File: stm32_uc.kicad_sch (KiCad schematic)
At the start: 13 parts, among them U1 STM32F103C8T6

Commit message: updated pdb
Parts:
- renumbered U1 to U?
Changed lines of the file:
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@@
   (symbol (lib_id "MCU_ST_STM32F1:STM32F103C8Tx") (at 139.7 100.33 0) (unit 1)
     (in_bom yes) (on_board yes)
-    (property "Reference" "U1" (id 0) (at 149.86 63.5 0)
+    (property "Reference" "U?" (id 0) (at 149.86 63.5 0)
       (effects (font (size 1.27 1.27)) (justify left))
     )
@@
     )
     (path "/780076de-fb73-43f2-b5aa-1c95059ff25d"
-      (reference "U1") (unit 1) (value "STM32F103C8T6") (footprint "Package_QFP:LQFP-48_7x7mm_P0.5mm")
-    )
-  )
+      (reference "U?") (unit 1) (value "STM32F103C8T6") (footprint "Package_QFP:LQFP-48_7x7mm_P0.5mm")
+    )
+  )

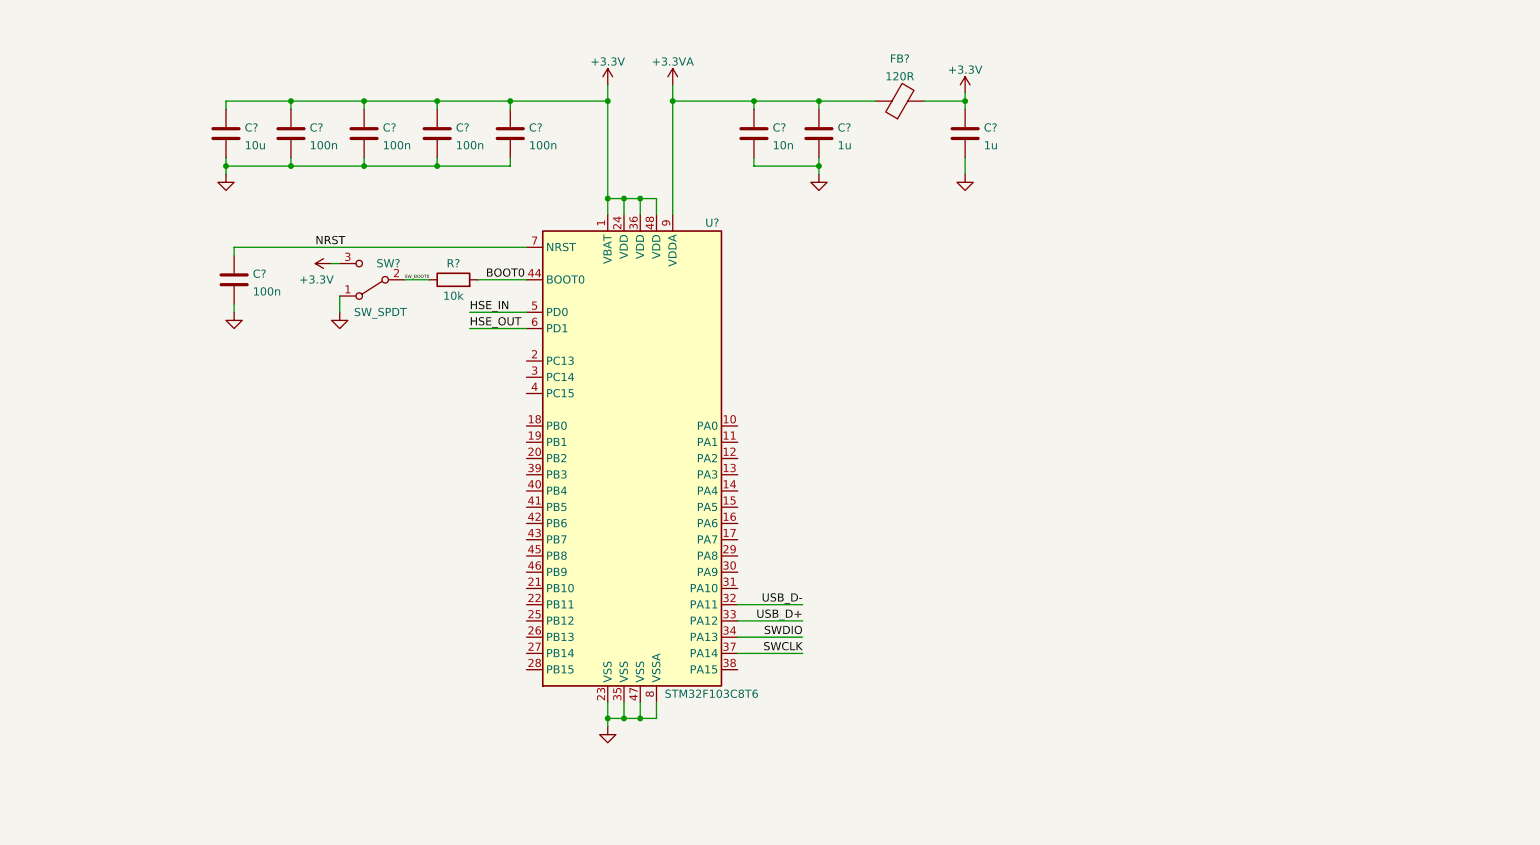
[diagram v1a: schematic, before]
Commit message: added power circuitry
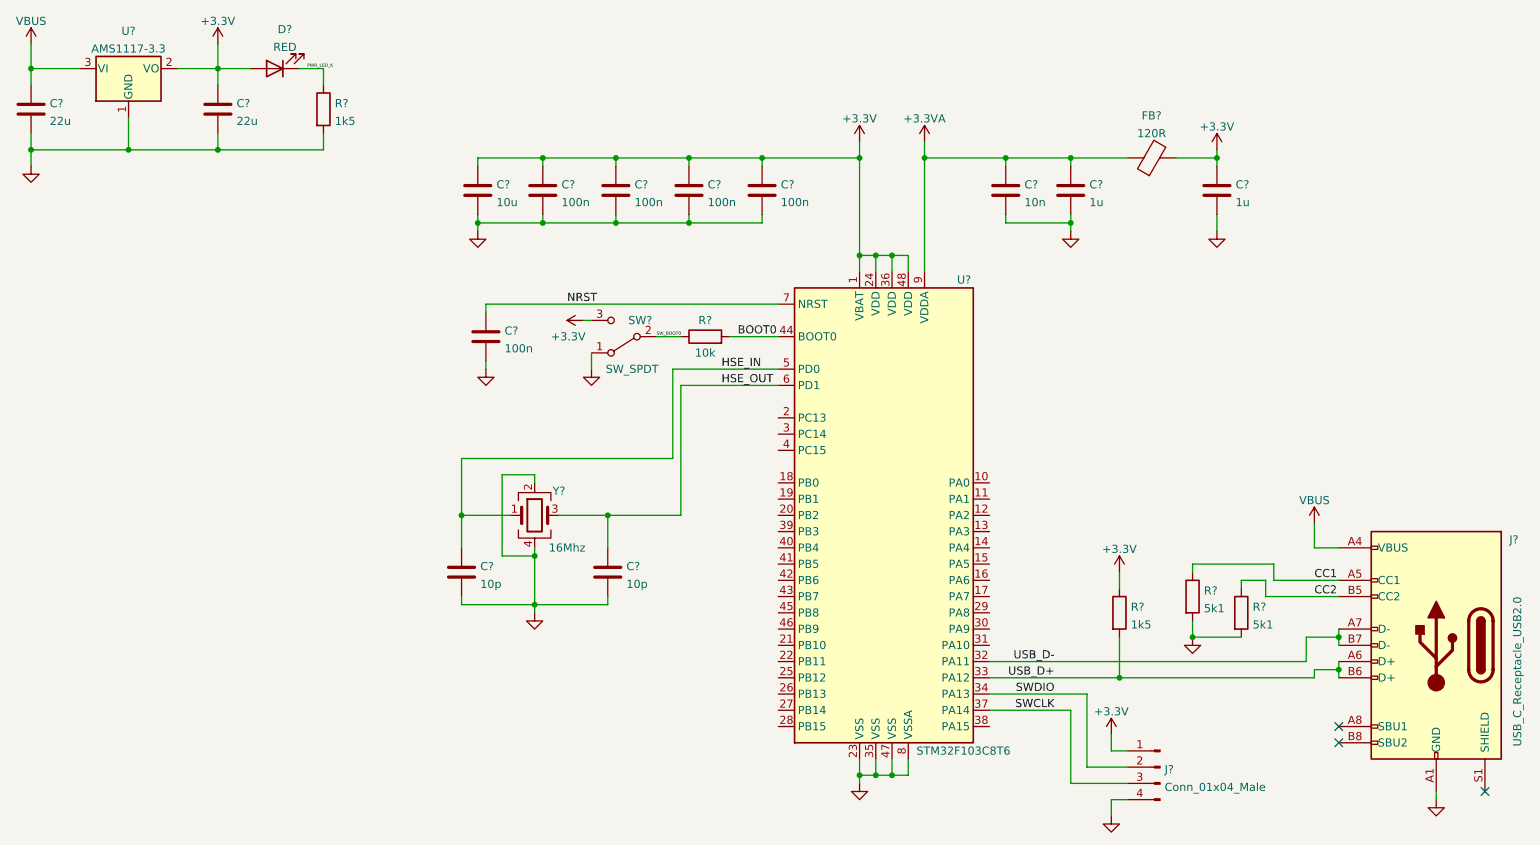
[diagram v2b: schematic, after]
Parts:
- added C? (x2): 22u, symbol Device:C
- added C? (x2): 10p, symbol Device:C
- added D?: RED, symbol Device:LED
- added J?: Conn_01x04_Male, symbol Connector:Conn_01x04_Male
- added J?: USB_C_Receptacle_USB2.0, symbol Connector:USB_C_Receptacle_USB2.0
- added R? (x2): 5k1, symbol Device:R
- added R? (x2): 1k5, symbol Device:R
- added U?: AMS1117-3.3, Package_TO_SOT_SMD:SOT-223-3_TabPin2, symbol Regulator_Linear:AMS1117-3.3
- added Y?: 16Mhz, symbol Device:Crystal_GND24
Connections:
- net +3V3: now also C?.1, D?.2 (A), J?.1 (Pin_1), R?.1, U?.2 (VO)
- net GND: now also C?.2, C?.2, C?.2, C?.2, J?.4 (Pin_4), J?.A1 (GND), J?.A12 (GND), J?.B1 (GND), J?.B12 (GND), R?.2, R?.2, R?.2, U?.1 (GND), Y?.2, Y?.4
- net HSE_IN: now also C?.1, Y?.1
- net HSE_OUT: now also C?.1, Y?.3
- net SWCLK: now also J?.3 (Pin_3)
- net SWDIO: now also J?.2 (Pin_2)
- net USB_D+: now also J?.A6 (D+), J?.B6 (D+), R?.2
- net USB_D-: now also J?.A7 (D-), J?.B7 (D-)
- new net CC1: J?.A5 (CC1), R?.1
- new net CC2: J?.B5 (CC2), R?.1
- new net PWR_LED_K: D?.1 (K), R?.1
- new net VBUS: C?.1, J?.A4 (VBUS), J?.A9 (VBUS), J?.B4 (VBUS), J?.B9 (VBUS), U?.3 (VI)
- no-connect marks 0 -> 3
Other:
- moved on the sheet: C?, FB?, R?, SW?, U?
